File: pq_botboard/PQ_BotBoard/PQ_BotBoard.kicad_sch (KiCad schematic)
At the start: 15 parts, among them IC3 TCN75AVUA713, J4 53261-0271, J5 533980671, J9 53261-1471

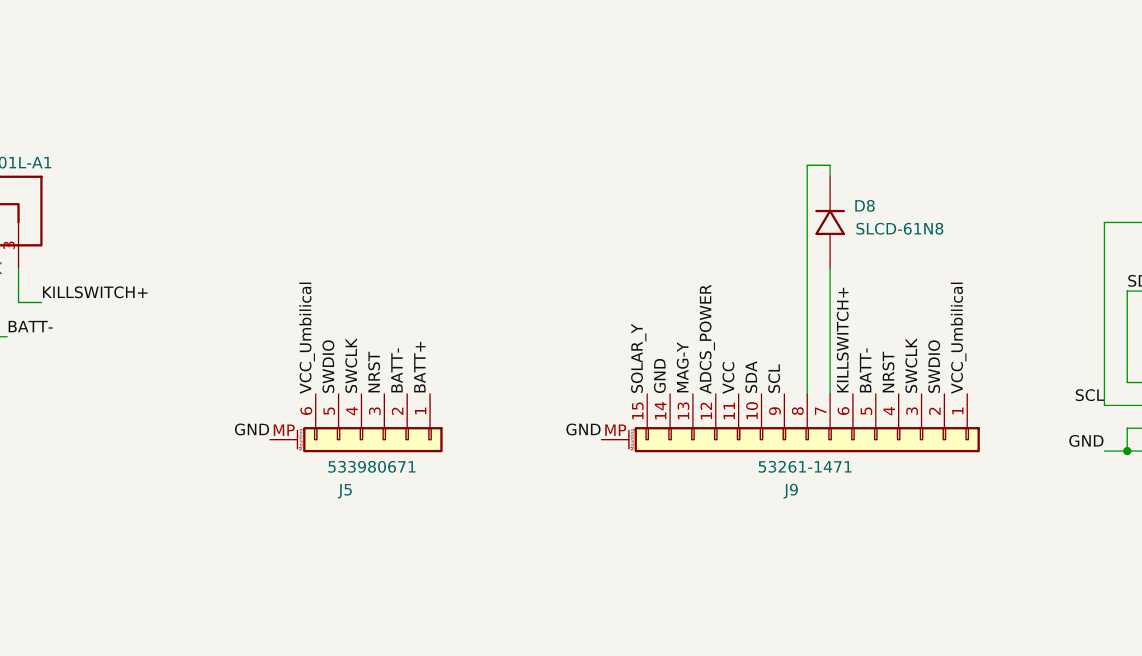
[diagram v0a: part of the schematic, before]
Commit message: killswitch and batt- pins swapped
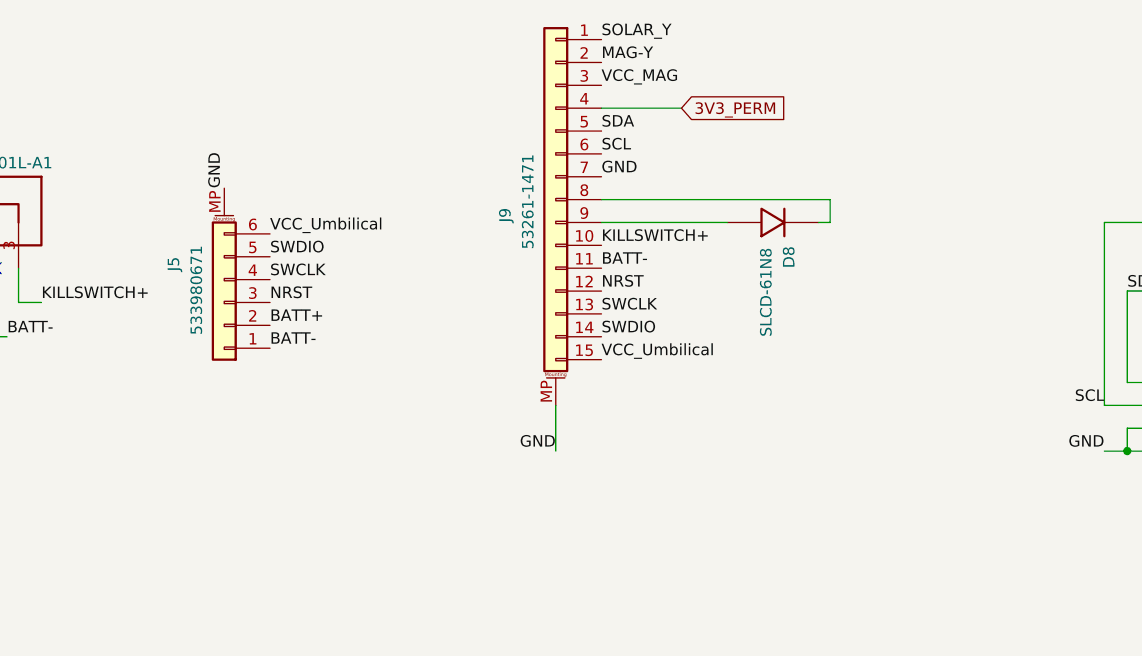
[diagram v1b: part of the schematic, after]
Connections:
- net ADCS_POWER is gone; now on net NRST: J9.12 (Pin_12)
- net BATT+: now also J5.2 (Pin_2); no longer J5.1 (Pin_1)
- net BATT-: now also J5.1 (Pin_1), J9.11 (Pin_11); no longer J5.2 (Pin_2), J9.5 (Pin_5)
- net GND: now also J9.7 (Pin_7); no longer J9.14 (Pin_14)
- net KILLSWITCH+: now also J9.10 (Pin_10); no longer J9.6 (Pin_6)
- net MAG-Y: now also J9.2 (Pin_2); no longer J9.13 (Pin_13)
- net NRST: no longer J9.4 (Pin_4)
- net SCL: now also J9.6 (Pin_6); no longer J9.9 (Pin_9)
- net SDA: now also J9.5 (Pin_5); no longer J9.10 (Pin_10)
- net SOLAR_Y: now also J9.1 (Pin_1); no longer J9.15 (Pin_15)
- net SWCLK: now also J9.13 (Pin_13); no longer J9.3 (Pin_3)
- net SWDIO: now also J9.14 (Pin_14); no longer J9.2 (Pin_2)
- net VCC: no longer J9.11 (Pin_11)
- net VCC_Umbilical: now also J9.15 (Pin_15); no longer J9.1 (Pin_1)
- net at D8.2: now also J9.9 (Pin_9); no longer J9.7 (Pin_7)
- new net 3V3_PERM: J9.4 (Pin_4)
- new net VCC_MAG: J9.3 (Pin_3)
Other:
- moved on the sheet: D8, J5, J9

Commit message: files changed
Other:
- note added: "Change temperature sensor footprint Battery connector Delete pull-ups"
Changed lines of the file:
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@@
     (stroke (width 0.254) (type default) (color 0 0 0 0))
+  )
+  (text "Change temperature sensor footprint\nBattery connector\nDelete pull-ups"
+    (at 180.34 175.26 0)
+    (effects (font (size 1.27 1.27)) (justify left bottom))
   )
   (label "GND" (at 105.41 71.12 90)

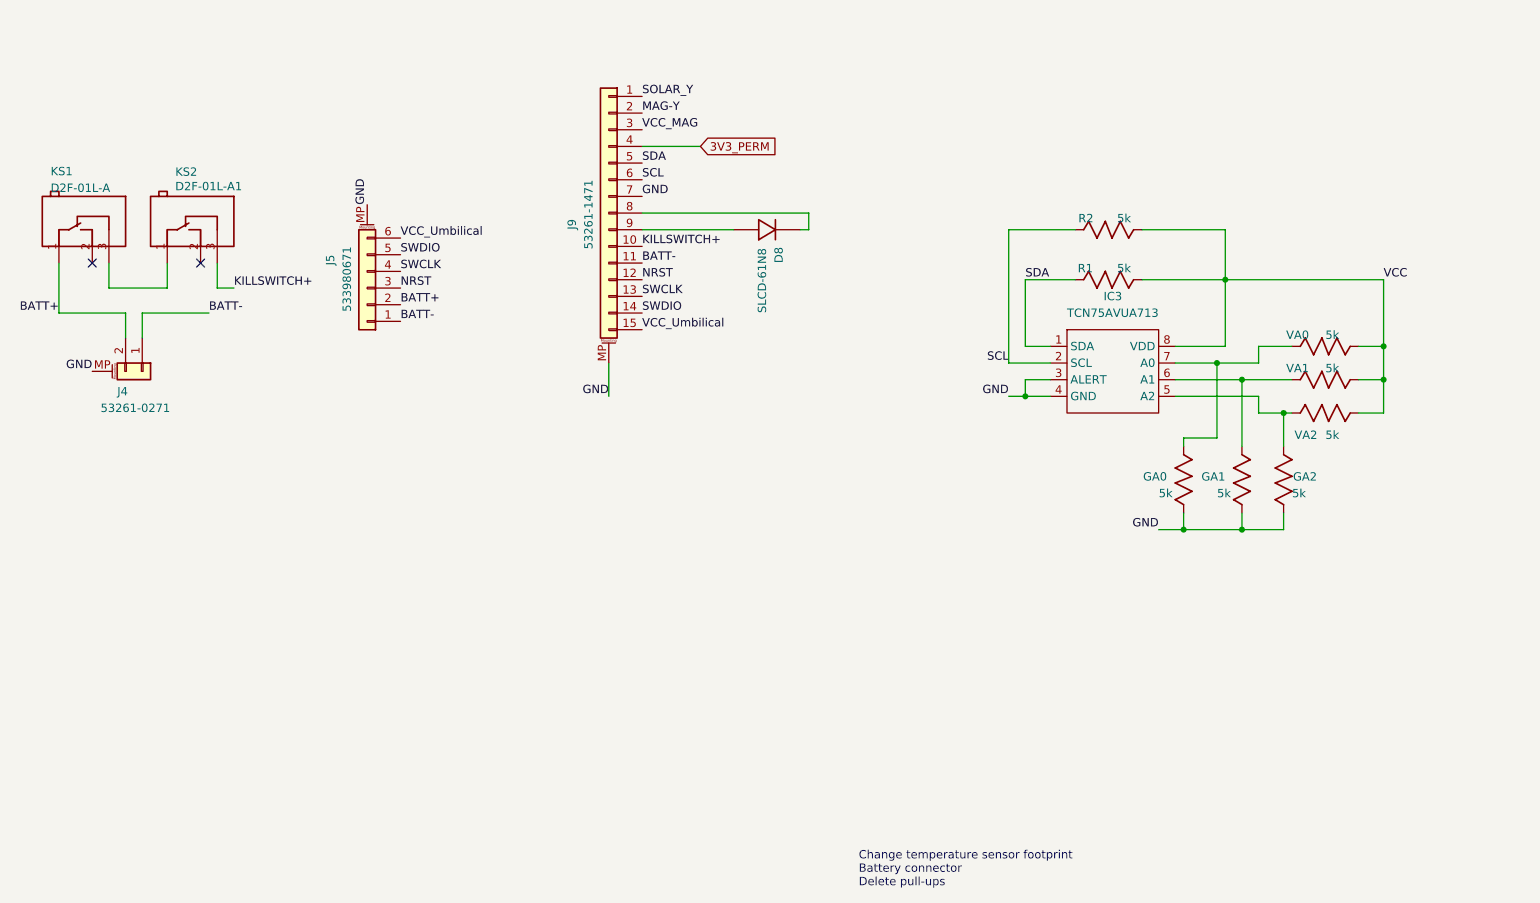
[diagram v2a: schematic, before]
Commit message: Lateral, Bottom and MagY boards done
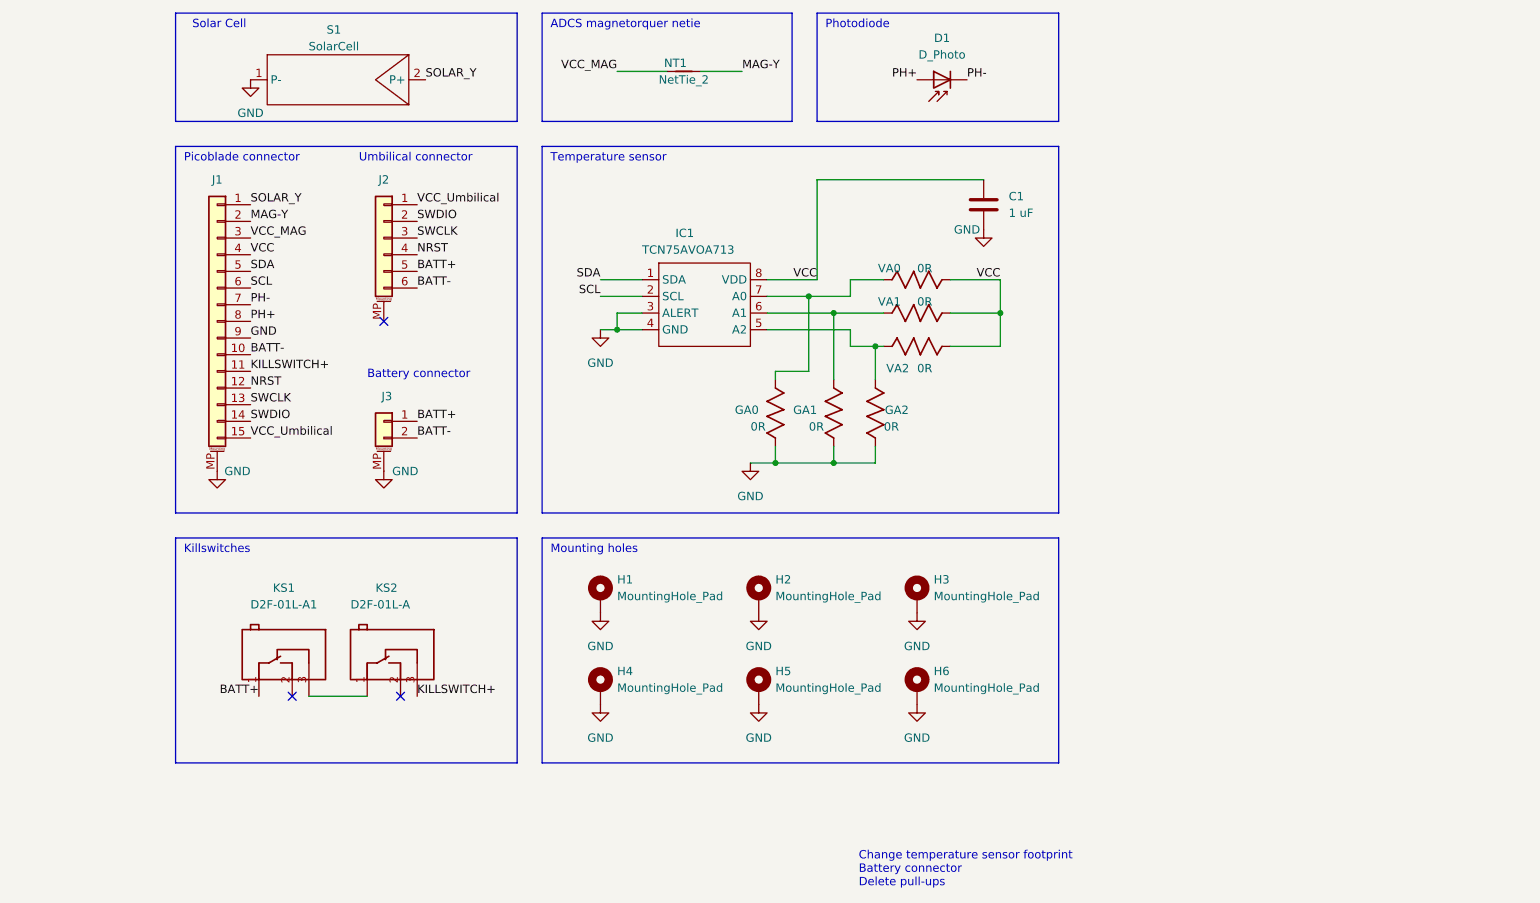
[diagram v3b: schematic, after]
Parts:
- removed D8: SLCD-61N8, SOD-123_L2.8-W1.8-LS3.7-RD, symbol Bottom_board-altium-import:0_SLCD-61N8
- removed GA0, GA1, GA2: 5k, R0805, symbol Bottom_board-altium-import:1_5k
- removed IC3: TCN75AVUA713, Package_SO:SOP-8_3.9x4.9mm_P1.27mm, symbol SP_ICs:TCN75AVUA713
- removed R1, R2, VA0, VA1, VA2: 5k, R0805, symbol Bottom_board-altium-import:0_5k
- added C1: 1 uF, Capacitor_SMD:C_0603_1608Metric, symbol Device:C
- added D1: D_Photo, NSL_misc:SLCD-61N8, symbol Device:D_Photo
- added GA0, GA1, GA2: 0R, Resistor_SMD:R_0805_2012Metric, symbol Lateral_board-altium-import:1_5k
- added H1, H2, H3, H4, H5, H6: MountingHole_Pad, MountingHole:MountingHole_2.2mm_M2_Pad, symbol Mechanical:MountingHole_Pad
- added IC1: TCN75AVOA713, Package_SO:SOP-8_3.9x4.9mm_P1.27mm, symbol SP_ICs:TCN75AVUA713
- added NT1: NetTie_2, NetTie:NetTie-2_SMD_Pad0.5mm, symbol Device:NetTie_2
- added S1: SolarCell, NSL_power:Solar_Cell, symbol NSL_power:SolarCell
- added VA0, VA1, VA2: 0R, Resistor_SMD:R_0805_2012Metric, symbol Lateral_board-altium-import:0_5k
- J1: renamed from J9; footprint CONN-SMD_532611471 -> Connector_Molex:Molex_PicoBlade_53261-1571_1x15-1MP_P1.25mm_Horizontal
- J2: renamed from J5; footprint CONN-SMD_6P-P1.25-V-M_533980671 -> Connector_Molex:Molex_PicoBlade_53398-0671_1x06-1MP_P1.25mm_Vertical
- J3: renamed from J4; footprint CONN-SMD_532610271 -> Connector_Molex:Molex_PicoBlade_53261-0271_1x02-1MP_P1.25mm_Horizontal
- KS1: value D2F-01L-A -> D2F-01L-A1; footprint SW-TH_D2F-01L -> SamacSys_Parts:D2FLA1
- KS2: value D2F-01L-A1 -> D2F-01L-A; footprint SW-TH_D2F-01L -> SamacSys_Parts:D2FLA
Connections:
- net 3V3_PERM is gone; now on net VCC: J1.4 (Pin_4)
- net BATT+: now also J2.5 (Pin_5), J3.1 (Pin_1); no longer J2.2 (Pin_2), J3.2 (Pin_2)
- net BATT-: now also J1.10 (Pin_10), J2.6 (Pin_6), J3.2 (Pin_2); no longer J1.11 (Pin_11), J2.1 (Pin_1), J3.1 (Pin_1)
- net GND: now also J1.9 (Pin_9), C1.2, GA0.1, GA1.1, GA2.1, H1.1, H2.1, H3.1, H4.1, H5.1, H6.1, IC1.3 (ALERT), IC1.4 (GND), S1.1 (P-); no longer J1.7 (Pin_7), J2.MP (MountPin)
- net KILLSWITCH+: now also J1.11 (Pin_11); no longer J1.10 (Pin_10)
- net MAG-Y: now also NT1.2
- net NRST: now also J2.4 (Pin_4); no longer J2.3 (Pin_3)
- net SCL: now also IC1.2 (SCL)
- net SDA: now also IC1.1 (SDA)
- net SOLAR_Y: now also S1.2 (P+)
- net SWCLK: now also J2.3 (Pin_3); no longer J2.4 (Pin_4)
- net SWDIO: now also J2.2 (Pin_2); no longer J2.5 (Pin_5)
- net VCC: now also C1.1, IC1.8 (VDD), VA0.2, VA1.2, VA2.2
- net VCC_MAG: now also NT1.1
- net VCC_Umbilical: now also J2.1 (Pin_1); no longer J2.6 (Pin_6)
- net PH+: now reaches J1.8 (Pin_8)
- net PH+: now also D1.2 (A)
- new net: GA0.2, IC1.7 (A0), VA0.1
- new net: GA2.2, IC1.5 (A2), VA2.1
- new net: GA1.2, IC1.6 (A1), VA1.1
- new net PH-: D1.1 (K), J1.7 (Pin_7)
- no-connect marks 2 -> 3
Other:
- note added: "ADCS magnetorquer netie"
- note added: "Battery connector"
- note added: "Killswitches"
- note added: "Mounting holes"
- note added: "Photodiode"
- note added: "Picoblade connector"
- note added: "Solar Cell"
- note added: "Temperature sensor"
- note added: "Umbilical connector"
- moved on the sheet: J1, J2, J3, KS1, KS2

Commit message: Functional revision and finishing touches part I
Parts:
- removed D1: D_Photo, NSL_misc:SLCD-61N8, symbol Device:D_Photo
- removed S1: SolarCell, NSL_power:Solar_Cell, symbol NSL_power:SolarCell
- added Annotation1: Silkscreen_Annotation, symbols-nsl:GRSS, symbol symbols-nsl:Silkscreen_Annotation
- added Annotation2: Silkscreen_Annotation, symbols-nsl:IEEE_logo, symbol symbols-nsl:Silkscreen_Annotation
- added Annotation3: Silkscreen_Annotation, symbols-nsl:UPC_positiu, symbol symbols-nsl:Silkscreen_Annotation
- added Annotation4: Silkscreen_Annotation, symbols-nsl:Telecos, symbol symbols-nsl:Silkscreen_Annotation
- added Annotation5: Silkscreen_Annotation, symbols-nsl:Bridgemaker, symbol symbols-nsl:Silkscreen_Annotation
- added D1: SLCD-61N8, passive-nsl:SLCD-61N8, symbol passive-nsl:SLCD-61N8
- added SC1: Solar_Cell, power-nsl:Azur-Space-PQ-cut-SC, symbol power-nsl:Solar_Cell
- KS1: footprint SamacSys_Parts:D2FLA1 -> miscelaneous-nsl:D2FLA1
- KS2: footprint SamacSys_Parts:D2FLA -> miscelaneous-nsl:D2FLA
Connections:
- net GND: now also SC1.1 (-)
- net PH+: now also D1.1
- net PH-: now also D1.2
- net SOLAR_Y: now also SC1.2
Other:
- note added: "Logos"
- note removed: "Change temperature sensor footprint Battery connector Delete pull-ups"

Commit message: Full Kicad7 transition, library improvement and adaptation, correct footprints and 3D models added
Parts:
- Annotation1: footprint symbols-nsl:GRSS -> -nsl_symbols:GRSS
- Annotation2: footprint symbols-nsl:IEEE_logo -> -nsl_symbols:IEEE_logo
- Annotation3: footprint symbols-nsl:UPC_positiu -> -nsl_symbols:UPC_positiu
- Annotation4: footprint symbols-nsl:Telecos -> -nsl_symbols:Telecos
- Annotation5: footprint symbols-nsl:Bridgemaker -> -nsl_symbols:Bridgemaker
- D1: footprint passive-nsl:SLCD-61N8 -> -nsl_passive:SLCD-61N8
- IC1: footprint Package_SO:SOP-8_3.9x4.9mm_P1.27mm -> -nsl_sensor:TCN75AVOA
- KS1: footprint miscelaneous-nsl:D2FLA1 -> -nsl_miscellaneous:D2FLA1
- KS2: footprint miscelaneous-nsl:D2FLA -> -nsl_miscellaneous:D2FLA
- SC1: footprint power-nsl:Azur-Space-PQ-cut-SC -> -nsl_power:Azur-Space-PQ-cut-SC

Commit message: fabrication
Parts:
- removed J2: 533980671, Connector_Molex:Molex_PicoBlade_53398-0671_1x06-1MP_P1.25mm_Vertical, symbol Connector_Generic_MountingPin:Conn_01x06_MountingPin
- added J2: Conn_01x08_MountingPin, Connector_Molex:Molex_PicoBlade_53398-0871_1x08-1MP_P1.25mm_Vertical, symbol Connector_Generic_MountingPin:Conn_01x08_MountingPin
- added NT2: NetTie_2, NetTie:NetTie-2_SMD_Pad0.5mm, symbol Device:NetTie_2
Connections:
- net BATT+: now also J2.6 (Pin_6)
- net BATT-: now also J2.7 (Pin_7)
- net GND: now also J1.7 (Pin_7), J2.8 (Pin_8), J2.MP (MountPin), NT2.2; no longer J1.9 (Pin_9)
- net NRST: now also J2.5 (Pin_5)
- net PH-: now also NT2.1; no longer J1.7 (Pin_7)
- net SWCLK: now also J2.3 (Pin_3)
- net SWDIO: now also J2.2 (Pin_2)
- net VCC_Umbilical: now also J2.1 (Pin_1)
- new net SWO: J1.9 (Pin_9), J2.4 (Pin_4)
- no-connect marks 3 -> 2
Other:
- note added: "Net-ties"
- note removed: "ADCS magnetorquer netie"
- moved on the sheet: Annotation1, Annotation2, Annotation3, Annotation4, Annotation5, C1, D1, GA0, GA1, GA2, IC1, NT1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

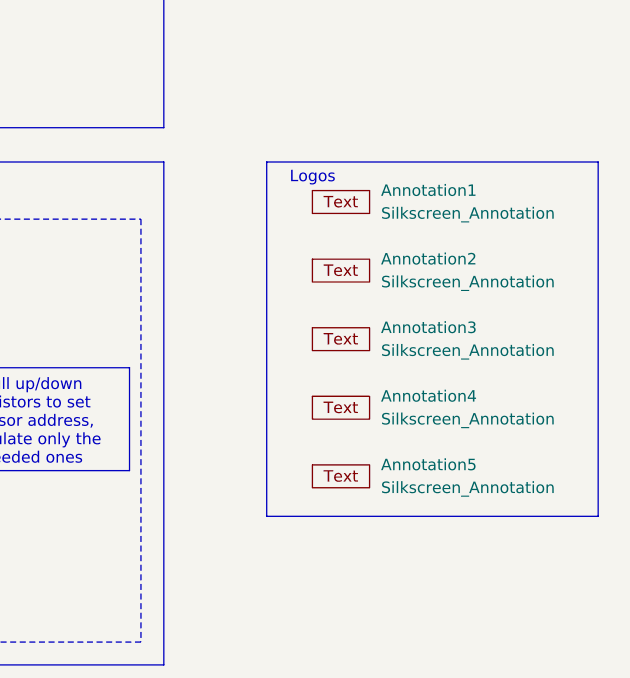
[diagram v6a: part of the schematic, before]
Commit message: Small changes of component fields for the BOM
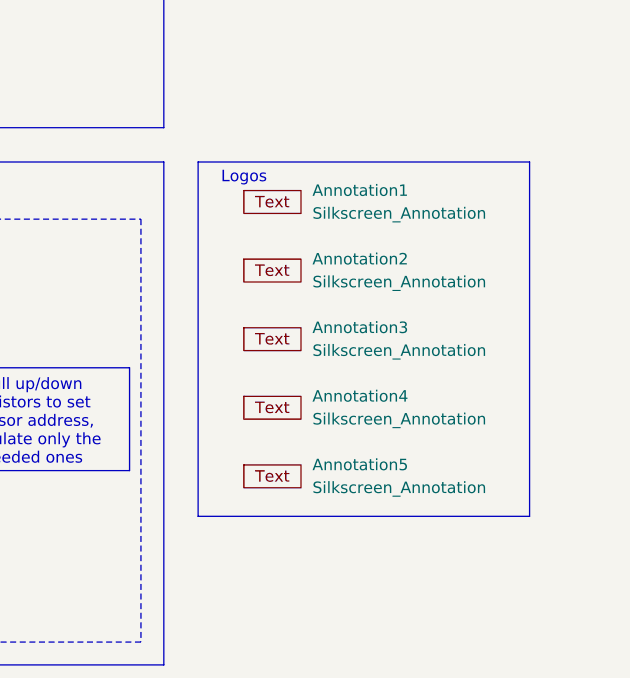
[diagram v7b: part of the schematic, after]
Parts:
- GA0, GA1, GA2, VA0, VA1, VA2: Manufacturer 1 (none) -> Vishay / Dale; Manufacturer Part Number 1 (none) -> CRCW08055K00JNTA; Supplier 1 (none) -> Mouser; Supplier Part Number 1 (none) -> 71-CRCW0805J-5K
- J1: Manufacturer 1 (none) -> MOLEX; Manufacturer Part Number 1 (none) -> 532611471; Supplier 1 (none) -> LCSC; Supplier Part Number 1 (none) -> C505101
- J3: Manufacturer 1 (none) -> MOLEX; Manufacturer Part Number 1 (none) -> 532610271; Supplier 1 (none) -> LCSC; Supplier Part Number 1 (none) -> C189700
- KS1, KS2: Manufacturer 1 (none) -> Omron Electronics; Manufacturer Part Number 1 (none) -> D2F-01L; Supplier 1 (none) -> LCSC; Supplier Part Number 1 (none) -> C231335
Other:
- moved on the sheet: Annotation1, Annotation2, Annotation3, Annotation4, Annotation5
